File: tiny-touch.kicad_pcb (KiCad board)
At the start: 2 copper layers, 99.8 x 98.5 mm, 118 parts, among them IC1 STM32F072VBT6, Q1 DTC123J, SW1 SW_Push, U1 MCP1700-3002E_SOT23, U2 SRV05-4

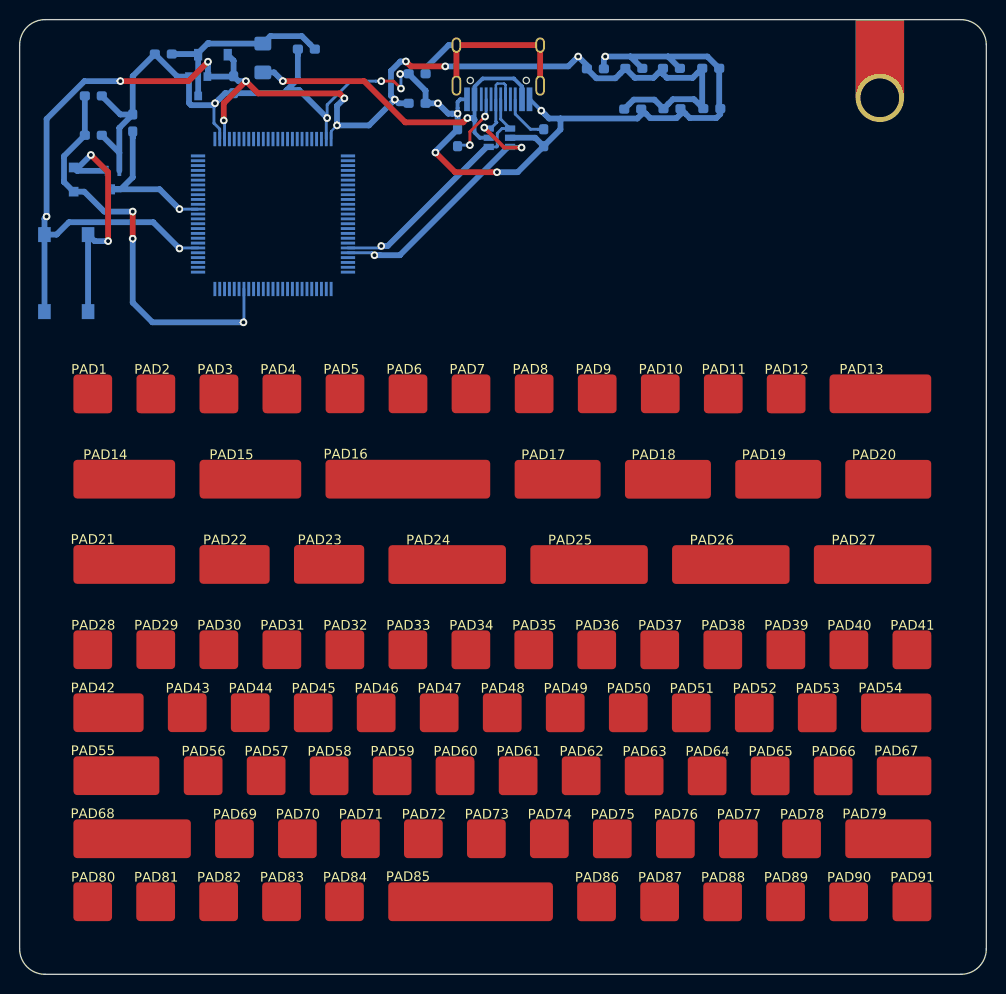
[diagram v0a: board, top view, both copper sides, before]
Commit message: Add all traces and gerbers for main board
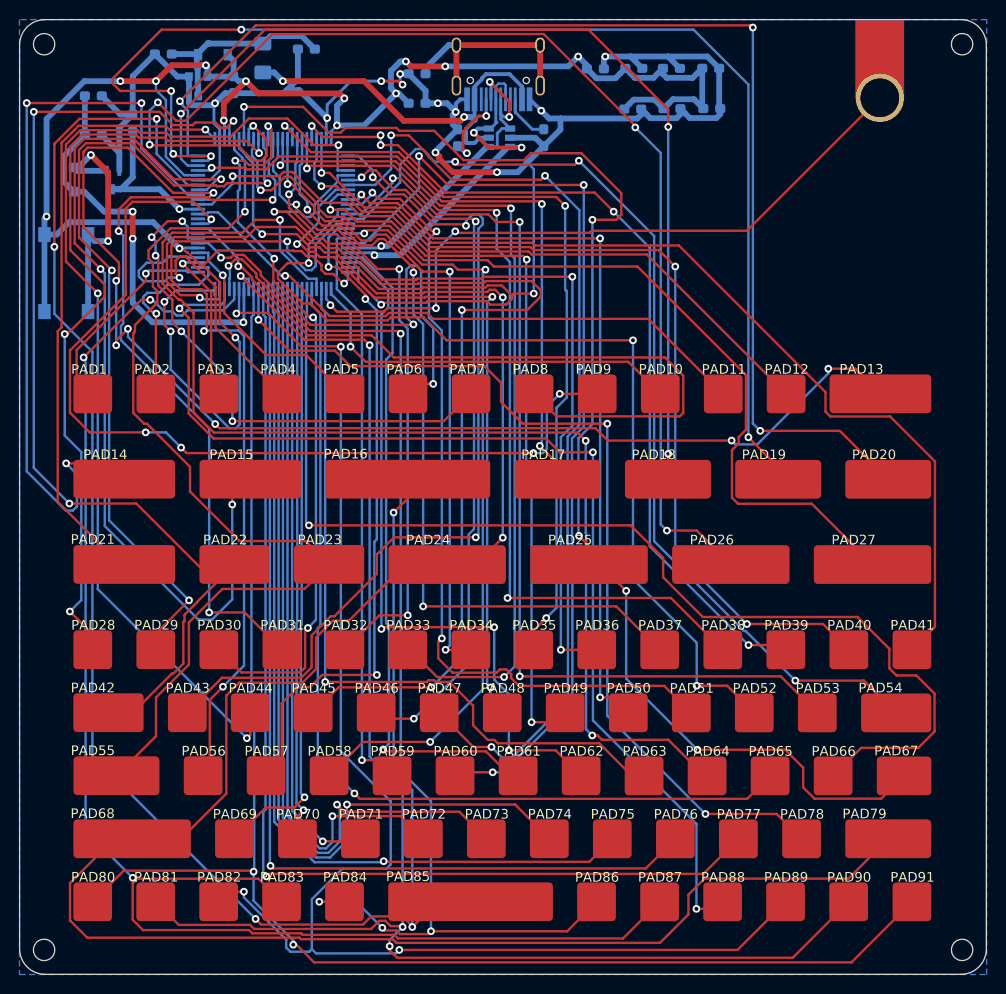
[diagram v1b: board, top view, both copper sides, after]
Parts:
- added HOLE1: MountingHole_2.2mm_M2, MountingHole:MountingHole_2.2mm_M2, F.Cu at (209.6, 43.7)
- added HOLE1: MountingHole_2.2mm_M2, MountingHole:MountingHole_2.2mm_M2, F.Cu at (114.8, 43.7)
- added HOLE1: MountingHole_2.2mm_M2, MountingHole:MountingHole_2.2mm_M2, F.Cu at (114.8, 137.2)
- added HOLE1: MountingHole_2.2mm_M2, MountingHole:MountingHole_2.2mm_M2, F.Cu at (209.6, 137.2)
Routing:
- net A6: track 0.00 -> 225.6 mm, vias 0 -> 3
- net F2: track 0.00 -> 181.4 mm, vias 0 -> 5
- net B7: track 0.00 -> 160.0 mm, vias 0 -> 4
- net B6: track 0.00 -> 155.2 mm, vias 0 -> 2
- net B9: track 0.00 -> 153.7 mm, vias 0 -> 3
- net B8: track 0.00 -> 150.1 mm, vias 0 -> 4
- net A7: track 0.00 -> 139.0 mm, vias 0 -> 5
- net C4: track 0.00 -> 131.9 mm, vias 0 -> 5
- net A1: track 0.00 -> 131.1 mm, vias 0 -> 5
- net C1: track 0.00 -> 129.0 mm, vias 0 -> 7
- net C11: track 0.00 -> 127.2 mm, vias 0 -> 3
- net A2: track 0.00 -> 126.8 mm, vias 0 -> 3
- net E0: track 0.00 -> 120.9 mm, vias 0 -> 5
- net E1: track 0.00 -> 115.4 mm, vias 0 -> 3
- net D0: track 0.00 -> 114.9 mm, vias 0 -> 1
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- added copper zone on B.Cu, net GND
